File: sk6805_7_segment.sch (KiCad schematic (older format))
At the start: 25 parts

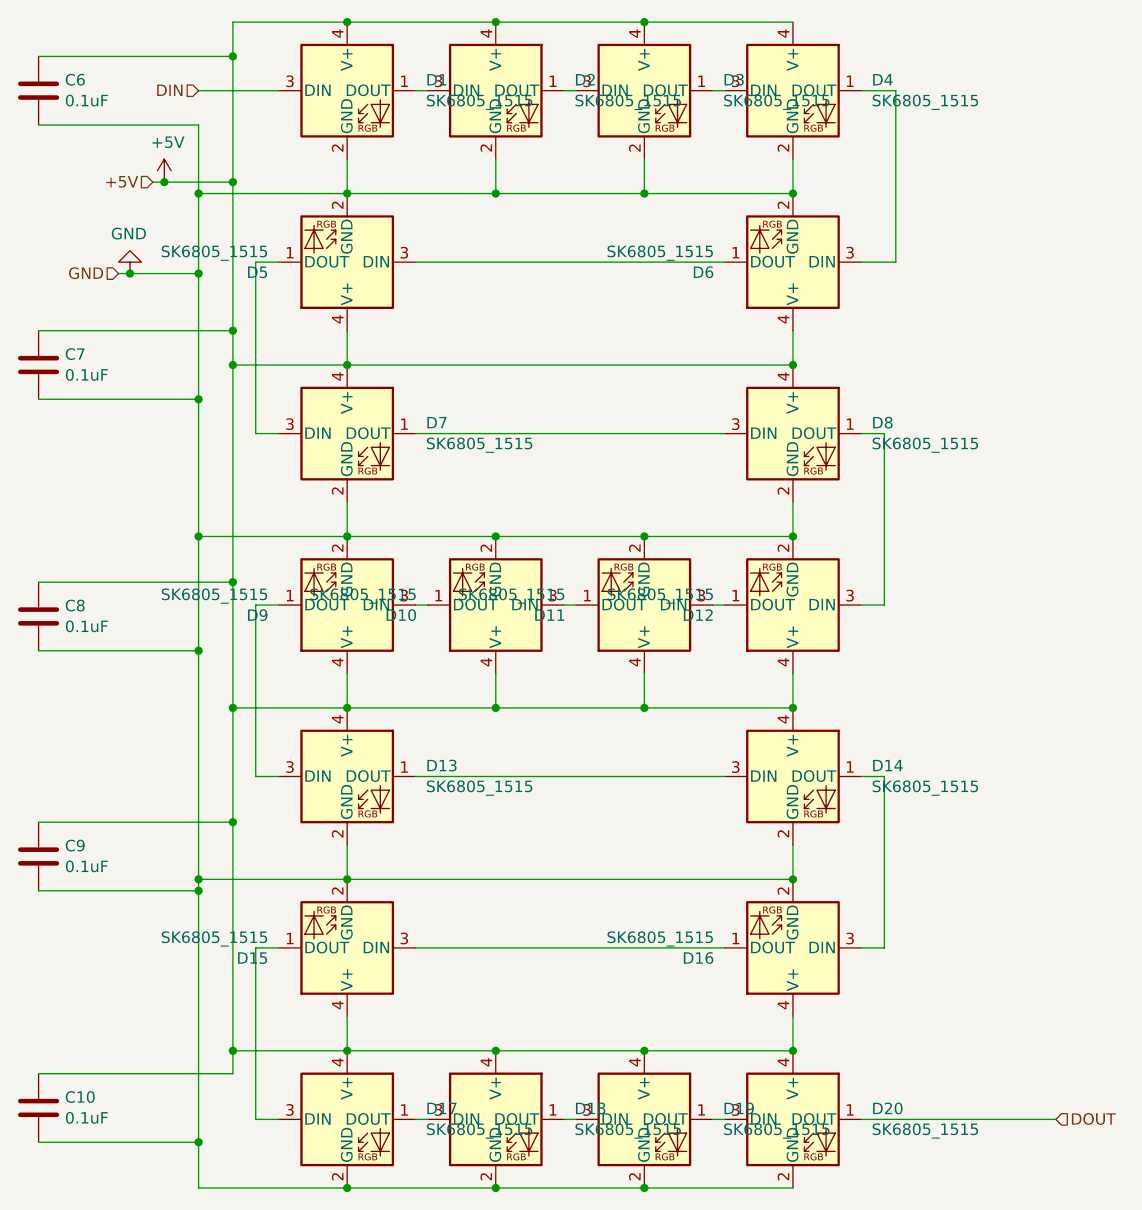
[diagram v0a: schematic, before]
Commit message: Add ISP header, wire up everything
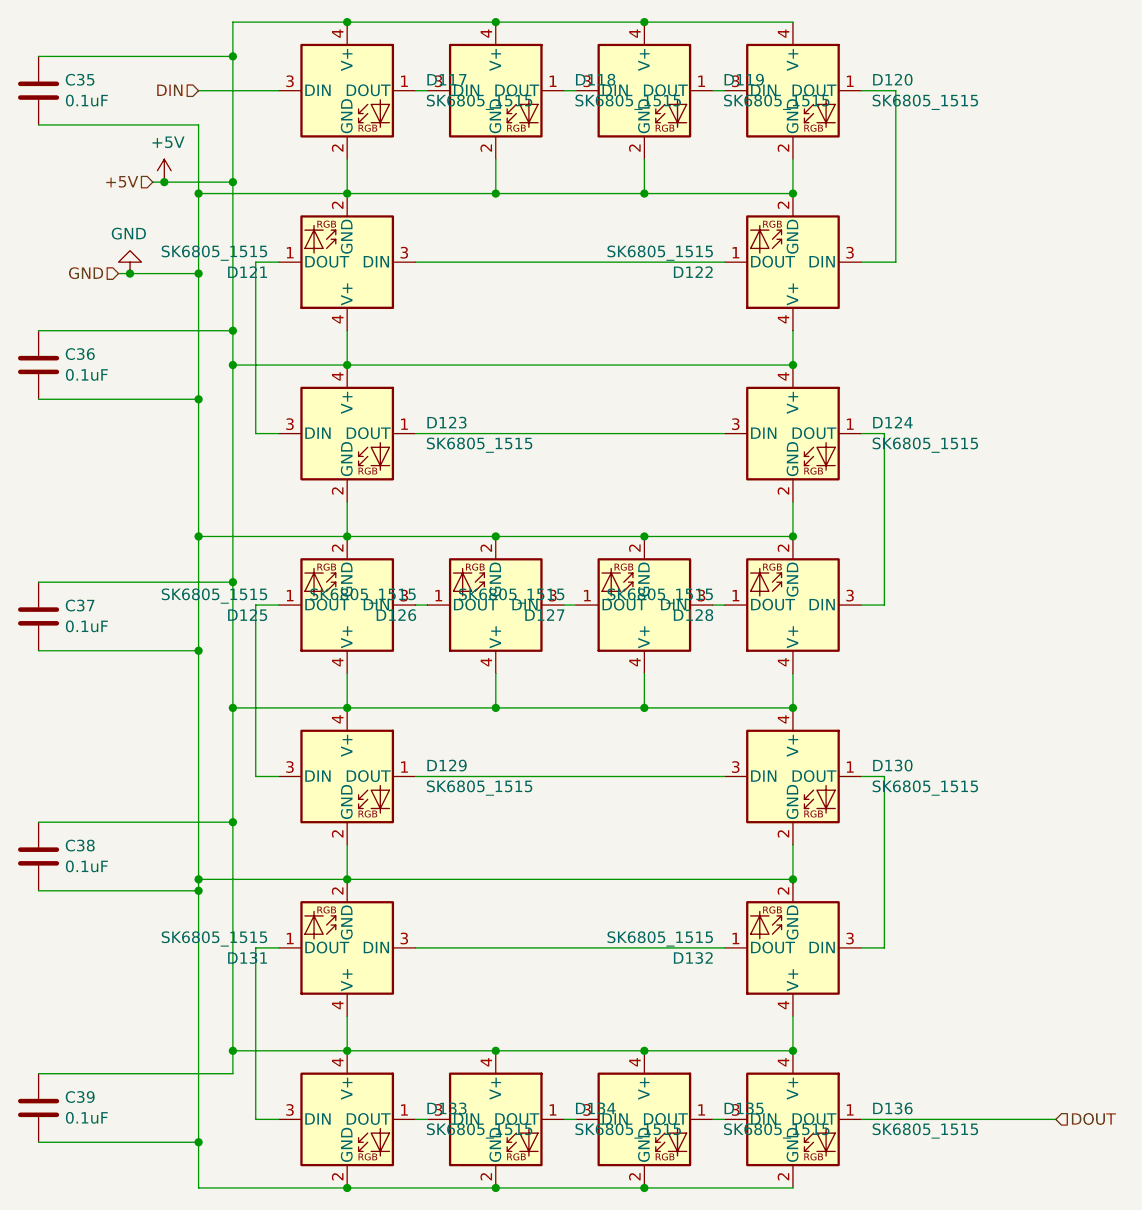
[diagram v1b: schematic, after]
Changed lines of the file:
@@
 AR Path="/5E94AF92/5E930F89" Ref="D12"  Part="1"
 AR Path="/5E94AF98/5E930F89" Ref="D32"  Part="1"
-F 0 "D12" H 6294 3196 50  0000 L CNN
+F 0 "D128" H 6294 3196 50  0000 L CNN
 F 1 "SK6805_1515" H 6294 3105 50  0000 L CNN
 F 2 "LED_SMD:LED_SK6805_PLCC4_1.5x1.5mm_P0.65mm" H 6000 2850 50  0001 L TNN
@@
 AR Path="/5E94AF92/5E930F8F" Ref="D11"  Part="1"
 AR Path="/5E94AF98/5E930F8F" Ref="D31"  Part="1"
-F 0 "D11" H 5644 3196 50  0000 L CNN
+F 0 "D127" H 5644 3196 50  0000 L CNN
 F 1 "SK6805_1515" H 5644 3105 50  0000 L CNN
 F 2 "LED_SMD:LED_SK6805_PLCC4_1.5x1.5mm_P0.65mm" H 5350 2850 50  0001 L TNN
@@
 AR Path="/5E94AF92/5E930F95" Ref="D10"  Part="1"
 AR Path="/5E94AF98/5E930F95" Ref="D30"  Part="1"
-F 0 "D10" H 4994 3196 50  0000 L CNN
+F 0 "D126" H 4994 3196 50  0000 L CNN
 F 1 "SK6805_1515" H 4994 3105 50  0000 L CNN
 F 2 "LED_SMD:LED_SK6805_PLCC4_1.5x1.5mm_P0.65mm" H 4700 2850 50  0001 L TNN
@@
 AR Path="/5E94AF92/5E930F9B" Ref="D9"  Part="1"
 AR Path="/5E94AF98/5E930F9B" Ref="D29"  Part="1"
-F 0 "D9" H 4344 3196 50  0000 L CNN
+F 0 "D125" H 4344 3196 50  0000 L CNN
 F 1 "SK6805_1515" H 4344 3105 50  0000 L CNN
 F 2 "LED_SMD:LED_SK6805_PLCC4_1.5x1.5mm_P0.65mm" H 4050 2850 50  0001 L TNN
@@
 AR Path="/5E94AF92/5E945F60" Ref="D7"  Part="1"
 AR Path="/5E94AF98/5E945F60" Ref="D27"  Part="1"
-F 0 "D7" H 4344 2446 50  0000 L CNN
+F 0 "D123" H 4344 2446 50  0000 L CNN
 F 1 "SK6805_1515" H 4344 2355 50  0000 L CNN
 F 2 "LED_SMD:LED_SK6805_PLCC4_1.5x1.5mm_P0.65mm" H 4050 2100 50  0001 L TNN
@@
 AR Path="/5E94AF92/5E945F66" Ref="D8"  Part="1"
 AR Path="/5E94AF98/5E945F66" Ref="D28"  Part="1"
-F 0 "D8" H 6294 2446 50  0000 L CNN
+F 0 "D124" H 6294 2446 50  0000 L CNN
 F 1 "SK6805_1515" H 6294 2355 50  0000 L CNN
 F 2 "LED_SMD:LED_SK6805_PLCC4_1.5x1.5mm_P0.65mm" H 6000 2100 50  0001 L TNN
@@
 AR Path="/5E94AF92/5E935980" Ref="D14"  Part="1"
 AR Path="/5E94AF98/5E935980" Ref="D34"  Part="1"
-F 0 "D14" H 6294 3946 50  0000 L CNN
+F 0 "D130" H 6294 3946 50  0000 L CNN
 F 1 "SK6805_1515" H 6294 3855 50  0000 L CNN
 F 2 "LED_SMD:LED_SK6805_PLCC4_1.5x1.5mm_P0.65mm" H 6000 3600 50  0001 L TNN
@@
 AR Path="/5E94AF92/5E934F6A" Ref="D13"  Part="1"
 AR Path="/5E94AF98/5E934F6A" Ref="D33"  Part="1"
-F 0 "D13" H 4344 3946 50  0000 L CNN
+F 0 "D129" H 4344 3946 50  0000 L CNN
 F 1 "SK6805_1515" H 4344 3855 50  0000 L CNN
 F 2 "LED_SMD:LED_SK6805_PLCC4_1.5x1.5mm_P0.65mm" H 4050 3600 50  0001 L TNN
@@
 AR Path="/5E94AF92/5E932DC7" Ref="D20"  Part="1"
 AR Path="/5E94AF98/5E932DC7" Ref="D40"  Part="1"
-F 0 "D20" H 6294 5446 50  0000 L CNN
+F 0 "D136" H 6294 5446 50  0000 L CNN
 F 1 "SK6805_1515" H 6294 5355 50  0000 L CNN
 F 2 "LED_SMD:LED_SK6805_PLCC4_1.5x1.5mm_P0.65mm" H 6000 5100 50  0001 L TNN
@@
 AR Path="/5E94AF92/5E932DC1" Ref="D19"  Part="1"
 AR Path="/5E94AF98/5E932DC1" Ref="D39"  Part="1"
-F 0 "D19" H 5644 5446 50  0000 L CNN
+F 0 "D135" H 5644 5446 50  0000 L CNN
 F 1 "SK6805_1515" H 5644 5355 50  0000 L CNN
 F 2 "LED_SMD:LED_SK6805_PLCC4_1.5x1.5mm_P0.65mm" H 5350 5100 50  0001 L TNN
@@
 AR Path="/5E94AF92/5E932DBB" Ref="D18"  Part="1"
 AR Path="/5E94AF98/5E932DBB" Ref="D38"  Part="1"
-F 0 "D18" H 4994 5446 50  0000 L CNN
+F 0 "D134" H 4994 5446 50  0000 L CNN
 F 1 "SK6805_1515" H 4994 5355 50  0000 L CNN
 F 2 "LED_SMD:LED_SK6805_PLCC4_1.5x1.5mm_P0.65mm" H 4700 5100 50  0001 L TNN
@@
 AR Path="/5E94AF92/5E932DB5" Ref="D17"  Part="1"
 AR Path="/5E94AF98/5E932DB5" Ref="D37"  Part="1"
-F 0 "D17" H 4344 5446 50  0000 L CNN
+F 0 "D133" H 4344 5446 50  0000 L CNN
 F 1 "SK6805_1515" H 4344 5355 50  0000 L CNN
 F 2 "LED_SMD:LED_SK6805_PLCC4_1.5x1.5mm_P0.65mm" H 4050 5100 50  0001 L TNN
@@
 AR Path="/5E94AF92/5E94B9F8" Ref="D15"  Part="1"
 AR Path="/5E94AF98/5E94B9F8" Ref="D35"  Part="1"
-F 0 "D15" H 4344 4696 50  0000 L CNN
+F 0 "D131" H 4344 4696 50  0000 L CNN
 F 1 "SK6805_1515" H 4344 4605 50  0000 L CNN
 F 2 "LED_SMD:LED_SK6805_PLCC4_1.5x1.5mm_P0.65mm" H 4050 4350 50  0001 L TNN
@@
 AR Path="/5E94AF92/5E94B9FE" Ref="D16"  Part="1"
 AR Path="/5E94AF98/5E94B9FE" Ref="D36"  Part="1"
-F 0 "D16" H 6294 4696 50  0000 L CNN
+F 0 "D132" H 6294 4696 50  0000 L CNN
 F 1 "SK6805_1515" H 6294 4605 50  0000 L CNN
 F 2 "LED_SMD:LED_SK6805_PLCC4_1.5x1.5mm_P0.65mm" H 6000 4350 50  0001 L TNN
@@
 AR Path="/5E94AF92/5E92B065" Ref="D4"  Part="1"
 AR Path="/5E94AF98/5E92B065" Ref="D24"  Part="1"
-F 0 "D4" H 6294 946 50  0000 L CNN
+F 0 "D120" H 6294 946 50  0000 L CNN
 F 1 "SK6805_1515" H 6294 855 50  0000 L CNN
 F 2 "LED_SMD:LED_SK6805_PLCC4_1.5x1.5mm_P0.65mm" H 6000 600 50  0001 L TNN
@@
 AR Path="/5E94AF92/5E92B05F" Ref="D3"  Part="1"
 AR Path="/5E94AF98/5E92B05F" Ref="D23"  Part="1"
-F 0 "D3" H 5644 946 50  0000 L CNN
+F 0 "D119" H 5644 946 50  0000 L CNN
 F 1 "SK6805_1515" H 5644 855 50  0000 L CNN
 F 2 "LED_SMD:LED_SK6805_PLCC4_1.5x1.5mm_P0.65mm" H 5350 600 50  0001 L TNN
@@
 AR Path="/5E94AF92/5E9293AD" Ref="D2"  Part="1"
 AR Path="/5E94AF98/5E9293AD" Ref="D22"  Part="1"
-F 0 "D2" H 4994 946 50  0000 L CNN
+F 0 "D118" H 4994 946 50  0000 L CNN
 F 1 "SK6805_1515" H 4994 855 50  0000 L CNN
 F 2 "LED_SMD:LED_SK6805_PLCC4_1.5x1.5mm_P0.65mm" H 4700 600 50  0001 L TNN
@@
 AR Path="/5E94AF92/5E9275F2" Ref="D1"  Part="1"
 AR Path="/5E94AF98/5E9275F2" Ref="D21"  Part="1"
-F 0 "D1" H 4344 946 50  0000 L CNN
+F 0 "D117" H 4344 946 50  0000 L CNN
 F 1 "SK6805_1515" H 4344 855 50  0000 L CNN
 F 2 "LED_SMD:LED_SK6805_PLCC4_1.5x1.5mm_P0.65mm" H 4050 600 50  0001 L TNN
@@
 AR Path="/5E94AF92/5E934665" Ref="D5"  Part="1"
 AR Path="/5E94AF98/5E934665" Ref="D25"  Part="1"
-F 0 "D5" H 4344 1696 50  0000 L CNN
+F 0 "D121" H 4344 1696 50  0000 L CNN
 F 1 "SK6805_1515" H 4344 1605 50  0000 L CNN
 F 2 "LED_SMD:LED_SK6805_PLCC4_1.5x1.5mm_P0.65mm" H 4050 1350 50  0001 L TNN
@@
 AR Path="/5E94AF92/5E934084" Ref="D6"  Part="1"
 AR Path="/5E94AF98/5E934084" Ref="D26"  Part="1"
-F 0 "D6" H 6294 1696 50  0000 L CNN
+F 0 "D122" H 6294 1696 50  0000 L CNN
 F 1 "SK6805_1515" H 6294 1605 50  0000 L CNN
 F 2 "LED_SMD:LED_SK6805_PLCC4_1.5x1.5mm_P0.65mm" H 6000 1350 50  0001 L TNN
@@
 AR Path="/5E94AF92/5E9D018F" Ref="C6"  Part="1"
 AR Path="/5E94AF98/5E9D018F" Ref="C11"  Part="1"
-F 0 "C6" H 2765 946 50  0000 L CNN
+F 0 "C35" H 2765 946 50  0000 L CNN
 F 1 "0.1uF" H 2765 855 50  0000 L CNN
 F 2 "Capacitor_SMD:C_0805_2012Metric" H 2688 750 50  0001 C CNN
@@
 AR Path="/5E94AF92/5E9D1CB0" Ref="C7"  Part="1"
 AR Path="/5E94AF98/5E9D1CB0" Ref="C12"  Part="1"
-F 0 "C7" H 2765 2146 50  0000 L CNN
+F 0 "C36" H 2765 2146 50  0000 L CNN
 F 1 "0.1uF" H 2765 2055 50  0000 L CNN
 F 2 "Capacitor_SMD:C_0805_2012Metric" H 2688 1950 50  0001 C CNN
@@
 AR Path="/5E94AF92/5E9DA066" Ref="C8"  Part="1"
 AR Path="/5E94AF98/5E9DA066" Ref="C13"  Part="1"
-F 0 "C8" H 2765 3246 50  0000 L CNN
+F 0 "C37" H 2765 3246 50  0000 L CNN
 F 1 "0.1uF" H 2765 3155 50  0000 L CNN
 F 2 "Capacitor_SMD:C_0805_2012Metric" H 2688 3050 50  0001 C CNN
@@
 AR Path="/5E94AF92/5E9DAA64" Ref="C9"  Part="1"
 AR Path="/5E94AF98/5E9DAA64" Ref="C14"  Part="1"
-F 0 "C9" H 2765 4296 50  0000 L CNN
+F 0 "C38" H 2765 4296 50  0000 L CNN
 F 1 "0.1uF" H 2765 4205 50  0000 L CNN
 F 2 "Capacitor_SMD:C_0805_2012Metric" H 2688 4100 50  0001 C CNN
@@
 AR Path="/5E94AF92/5E9DAE95" Ref="C10"  Part="1"
 AR Path="/5E94AF98/5E9DAE95" Ref="C15"  Part="1"
-F 0 "C10" H 2765 5396 50  0000 L CNN
+F 0 "C39" H 2765 5396 50  0000 L CNN
 F 1 "0.1uF" H 2765 5305 50  0000 L CNN
 F 2 "Capacitor_SMD:C_0805_2012Metric" H 2688 5200 50  0001 C CNN

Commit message: Update usb position, byline
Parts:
- D117, D118, D119, D120, D121, D122, D123, D124, D125, D126, D127, D128, D129, D130, D131, D132, D133, D134, D135, D136: symbol LED:SK6805_1515 -> shadow_box_sk6805-rescue:SK6805_1515-LED
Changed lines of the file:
@@
 EESchema Schematic File Version 4
-LIBS:shadow_box_sk6805-cache
-EELAYER 29 0
+EELAYER 30 0
 EELAYER END
 $Descr A4 11693 8268
@@
 DOUT
 $Comp
-L LED:SK6805_1515 D128
+L shadow_box_sk6805-rescue:SK6805_1515-LED D128
 U 1 1 5E930F89
 P 5950 3150
@@
 AR Path="/5E94AF92/5E930F89" Ref="D12"  Part="1"
 AR Path="/5E94AF98/5E930F89" Ref="D32"  Part="1"
+AR Path="/5E930F89" Ref="D128"  Part="1"
 F 0 "D128" H 6294 3196 50  0000 L CNN
 F 1 "SK6805_1515" H 6294 3105 50  0000 L CNN
@@
 $EndComp
 $Comp
-L LED:SK6805_1515 D127
+L shadow_box_sk6805-rescue:SK6805_1515-LED D127
 U 1 1 5E930F8F
 P 5300 3150
@@
 AR Path="/5E94AF92/5E930F8F" Ref="D11"  Part="1"
 AR Path="/5E94AF98/5E930F8F" Ref="D31"  Part="1"
+AR Path="/5E930F8F" Ref="D127"  Part="1"
 F 0 "D127" H 5644 3196 50  0000 L CNN
 F 1 "SK6805_1515" H 5644 3105 50  0000 L CNN
@@
 $EndComp
 $Comp
-L LED:SK6805_1515 D126
+L shadow_box_sk6805-rescue:SK6805_1515-LED D126
 U 1 1 5E930F95
 P 4650 3150
@@
 AR Path="/5E94AF92/5E930F95" Ref="D10"  Part="1"
 AR Path="/5E94AF98/5E930F95" Ref="D30"  Part="1"
+AR Path="/5E930F95" Ref="D126"  Part="1"
 F 0 "D126" H 4994 3196 50  0000 L CNN
 F 1 "SK6805_1515" H 4994 3105 50  0000 L CNN
@@
 $EndComp
 $Comp
-L LED:SK6805_1515 D125
+L shadow_box_sk6805-rescue:SK6805_1515-LED D125
 U 1 1 5E930F9B
 P 4000 3150
@@
 AR Path="/5E94AF92/5E930F9B" Ref="D9"  Part="1"
 AR Path="/5E94AF98/5E930F9B" Ref="D29"  Part="1"
+AR Path="/5E930F9B" Ref="D125"  Part="1"
 F 0 "D125" H 4344 3196 50  0000 L CNN
 F 1 "SK6805_1515" H 4344 3105 50  0000 L CNN
@@
 $EndComp
 $Comp
-L LED:SK6805_1515 D123
+L shadow_box_sk6805-rescue:SK6805_1515-LED D123
 U 1 1 5E945F60
 P 4000 2400
@@
 AR Path="/5E94AF92/5E945F60" Ref="D7"  Part="1"
 AR Path="/5E94AF98/5E945F60" Ref="D27"  Part="1"
+AR Path="/5E945F60" Ref="D123"  Part="1"
 F 0 "D123" H 4344 2446 50  0000 L CNN
 F 1 "SK6805_1515" H 4344 2355 50  0000 L CNN
@@
 $EndComp
 $Comp
-L LED:SK6805_1515 D124
+L shadow_box_sk6805-rescue:SK6805_1515-LED D124
 U 1 1 5E945F66
 P 5950 2400
@@
 AR Path="/5E94AF92/5E945F66" Ref="D8"  Part="1"
 AR Path="/5E94AF98/5E945F66" Ref="D28"  Part="1"
+AR Path="/5E945F66" Ref="D124"  Part="1"
 F 0 "D124" H 6294 2446 50  0000 L CNN
 F 1 "SK6805_1515" H 6294 2355 50  0000 L CNN
@@
 $EndComp
 $Comp
-L LED:SK6805_1515 D130
+L shadow_box_sk6805-rescue:SK6805_1515-LED D130
 U 1 1 5E935980
 P 5950 3900
@@
 AR Path="/5E94AF92/5E935980" Ref="D14"  Part="1"
 AR Path="/5E94AF98/5E935980" Ref="D34"  Part="1"
+AR Path="/5E935980" Ref="D130"  Part="1"
 F 0 "D130" H 6294 3946 50  0000 L CNN
 F 1 "SK6805_1515" H 6294 3855 50  0000 L CNN
@@
 $EndComp
 $Comp
-L LED:SK6805_1515 D129
+L shadow_box_sk6805-rescue:SK6805_1515-LED D129
 U 1 1 5E934F6A
 P 4000 3900
@@
 AR Path="/5E94AF92/5E934F6A" Ref="D13"  Part="1"
 AR Path="/5E94AF98/5E934F6A" Ref="D33"  Part="1"
+AR Path="/5E934F6A" Ref="D129"  Part="1"
 F 0 "D129" H 4344 3946 50  0000 L CNN
 F 1 "SK6805_1515" H 4344 3855 50  0000 L CNN
@@
 $EndComp
 $Comp
-L LED:SK6805_1515 D136
+L shadow_box_sk6805-rescue:SK6805_1515-LED D136
 U 1 1 5E932DC7
 P 5950 5400
@@
 AR Path="/5E94AF92/5E932DC7" Ref="D20"  Part="1"
 AR Path="/5E94AF98/5E932DC7" Ref="D40"  Part="1"
+AR Path="/5E932DC7" Ref="D136"  Part="1"
 F 0 "D136" H 6294 5446 50  0000 L CNN
 F 1 "SK6805_1515" H 6294 5355 50  0000 L CNN
@@
 $EndComp
 $Comp
-L LED:SK6805_1515 D135
+L shadow_box_sk6805-rescue:SK6805_1515-LED D135
 U 1 1 5E932DC1
 P 5300 5400
@@
 AR Path="/5E94AF92/5E932DC1" Ref="D19"  Part="1"
 AR Path="/5E94AF98/5E932DC1" Ref="D39"  Part="1"
+AR Path="/5E932DC1" Ref="D135"  Part="1"
 F 0 "D135" H 5644 5446 50  0000 L CNN
 F 1 "SK6805_1515" H 5644 5355 50  0000 L CNN
@@
 $EndComp
 $Comp
-L LED:SK6805_1515 D134
+L shadow_box_sk6805-rescue:SK6805_1515-LED D134
 U 1 1 5E932DBB
 P 4650 5400
@@
 AR Path="/5E94AF92/5E932DBB" Ref="D18"  Part="1"
 AR Path="/5E94AF98/5E932DBB" Ref="D38"  Part="1"
+AR Path="/5E932DBB" Ref="D134"  Part="1"
 F 0 "D134" H 4994 5446 50  0000 L CNN
 F 1 "SK6805_1515" H 4994 5355 50  0000 L CNN
@@
 $EndComp
 $Comp
-L LED:SK6805_1515 D133
+L shadow_box_sk6805-rescue:SK6805_1515-LED D133
 U 1 1 5E932DB5
 P 4000 5400
@@
 AR Path="/5E94AF92/5E932DB5" Ref="D17"  Part="1"
 AR Path="/5E94AF98/5E932DB5" Ref="D37"  Part="1"
+AR Path="/5E932DB5" Ref="D133"  Part="1"
 F 0 "D133" H 4344 5446 50  0000 L CNN
 F 1 "SK6805_1515" H 4344 5355 50  0000 L CNN
@@
 $EndComp
 $Comp
-L LED:SK6805_1515 D131
+L shadow_box_sk6805-rescue:SK6805_1515-LED D131
 U 1 1 5E94B9F8
 P 4000 4650
@@
 AR Path="/5E94AF92/5E94B9F8" Ref="D15"  Part="1"
 AR Path="/5E94AF98/5E94B9F8" Ref="D35"  Part="1"
+AR Path="/5E94B9F8" Ref="D131"  Part="1"
 F 0 "D131" H 4344 4696 50  0000 L CNN
 F 1 "SK6805_1515" H 4344 4605 50  0000 L CNN
@@
 $EndComp
 $Comp
-L LED:SK6805_1515 D132
+L shadow_box_sk6805-rescue:SK6805_1515-LED D132
 U 1 1 5E94B9FE
 P 5950 4650
@@
 AR Path="/5E94AF92/5E94B9FE" Ref="D16"  Part="1"
 AR Path="/5E94AF98/5E94B9FE" Ref="D36"  Part="1"
+AR Path="/5E94B9FE" Ref="D132"  Part="1"
 F 0 "D132" H 6294 4696 50  0000 L CNN
 F 1 "SK6805_1515" H 6294 4605 50  0000 L CNN
@@
 	3150 1300 3200 1300
 $Comp
-L LED:SK6805_1515 D120
+L shadow_box_sk6805-rescue:SK6805_1515-LED D120
 U 1 1 5E92B065
 P 5950 900
@@
 AR Path="/5E94AF92/5E92B065" Ref="D4"  Part="1"
 AR Path="/5E94AF98/5E92B065" Ref="D24"  Part="1"
+AR Path="/5E92B065" Ref="D120"  Part="1"
 F 0 "D120" H 6294 946 50  0000 L CNN
 F 1 "SK6805_1515" H 6294 855 50  0000 L CNN
@@
 $EndComp
 $Comp
-L LED:SK6805_1515 D119
+L shadow_box_sk6805-rescue:SK6805_1515-LED D119
 U 1 1 5E92B05F
 P 5300 900
@@
 AR Path="/5E94AF92/5E92B05F" Ref="D3"  Part="1"
 AR Path="/5E94AF98/5E92B05F" Ref="D23"  Part="1"
+AR Path="/5E92B05F" Ref="D119"  Part="1"
 F 0 "D119" H 5644 946 50  0000 L CNN
 F 1 "SK6805_1515" H 5644 855 50  0000 L CNN
@@
 $EndComp
 $Comp
-L LED:SK6805_1515 D118
+L shadow_box_sk6805-rescue:SK6805_1515-LED D118
 U 1 1 5E9293AD
 P 4650 900
@@
 AR Path="/5E94AF92/5E9293AD" Ref="D2"  Part="1"
 AR Path="/5E94AF98/5E9293AD" Ref="D22"  Part="1"
+AR Path="/5E9293AD" Ref="D118"  Part="1"
 F 0 "D118" H 4994 946 50  0000 L CNN
 F 1 "SK6805_1515" H 4994 855 50  0000 L CNN
@@
 $EndComp
 $Comp
-L LED:SK6805_1515 D117
+L shadow_box_sk6805-rescue:SK6805_1515-LED D117
 U 1 1 5E9275F2
 P 4000 900
@@
 AR Path="/5E94AF92/5E9275F2" Ref="D1"  Part="1"
 AR Path="/5E94AF98/5E9275F2" Ref="D21"  Part="1"
+AR Path="/5E9275F2" Ref="D117"  Part="1"
 F 0 "D117" H 4344 946 50  0000 L CNN
 F 1 "SK6805_1515" H 4344 855 50  0000 L CNN
@@
 	5650 4650 4300 4650
 $Comp
-L LED:SK6805_1515 D121
+L shadow_box_sk6805-rescue:SK6805_1515-LED D121
 U 1 1 5E934665
 P 4000 1650
@@
 AR Path="/5E94AF92/5E934665" Ref="D5"  Part="1"
 AR Path="/5E94AF98/5E934665" Ref="D25"  Part="1"
+AR Path="/5E934665" Ref="D121"  Part="1"
 F 0 "D121" H 4344 1696 50  0000 L CNN
 F 1 "SK6805_1515" H 4344 1605 50  0000 L CNN
@@
 $EndComp
 $Comp
-L LED:SK6805_1515 D122
+L shadow_box_sk6805-rescue:SK6805_1515-LED D122
 U 1 1 5E934084
 P 5950 1650
@@
 AR Path="/5E94AF92/5E934084" Ref="D6"  Part="1"
 AR Path="/5E94AF98/5E934084" Ref="D26"  Part="1"
+AR Path="/5E934084" Ref="D122"  Part="1"
 F 0 "D122" H 6294 1696 50  0000 L CNN
 F 1 "SK6805_1515" H 6294 1605 50  0000 L CNN
